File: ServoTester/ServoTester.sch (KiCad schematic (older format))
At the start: 20 parts, among them P1 CONN_01X02, U1 TLC555, U2 TLC555, U3 AP3012

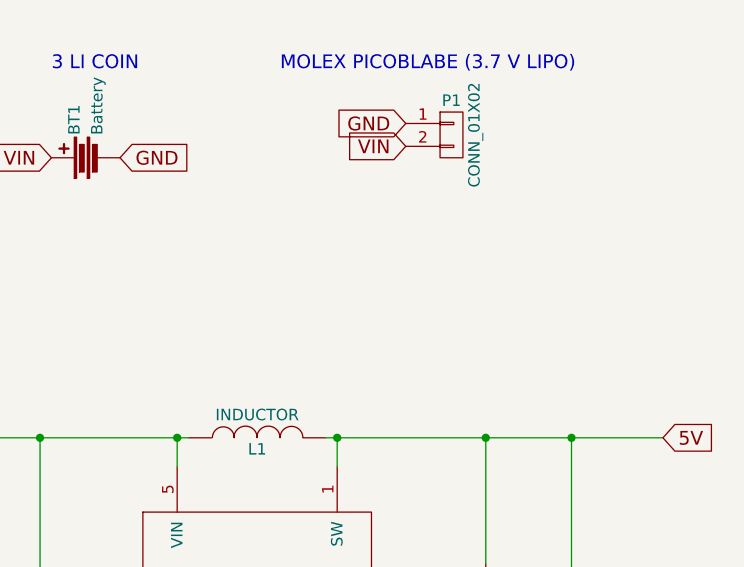
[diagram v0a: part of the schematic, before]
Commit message: fixed CKN
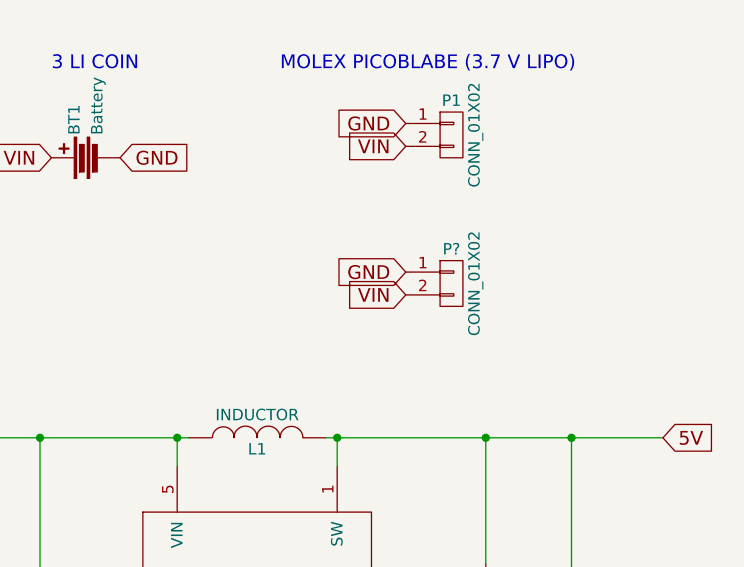
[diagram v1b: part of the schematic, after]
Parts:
- added P?: CONN_01X02, symbol CONN_01X02
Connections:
- net GND: now also P?.1 (P1)
- net VIN: now also P?.2 (P2)
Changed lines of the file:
@@
 Text Label 2975 4350 0    60   ~ 0
 PWM
+$Comp
+L CONN_01X02 P?
+U 1 1 5A1CD9E3
+P 9125 2600
+F 0 "P?" H 9125 2750 50  0000 C CNN
+F 1 "CONN_01X02" V 9225 2600 50  0000 C CNN
+F 2 "" H 9125 2600 50  0000 C CNN
+F 3 "" H 9125 2600 50  0000 C CNN
+	1    9125 2600
+	1    0    0    -1
+$EndComp
+Text GLabel 8925 2550 0    60   Input ~ 0
+GND
+Text GLabel 8925 2650 0    60   Input ~ 0
+VIN
 $EndSCHEMATC
